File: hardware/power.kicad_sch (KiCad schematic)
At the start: 21 parts, among them J1 PWR_IN 12V, Q9 TPN1R603PL, U2 78L05

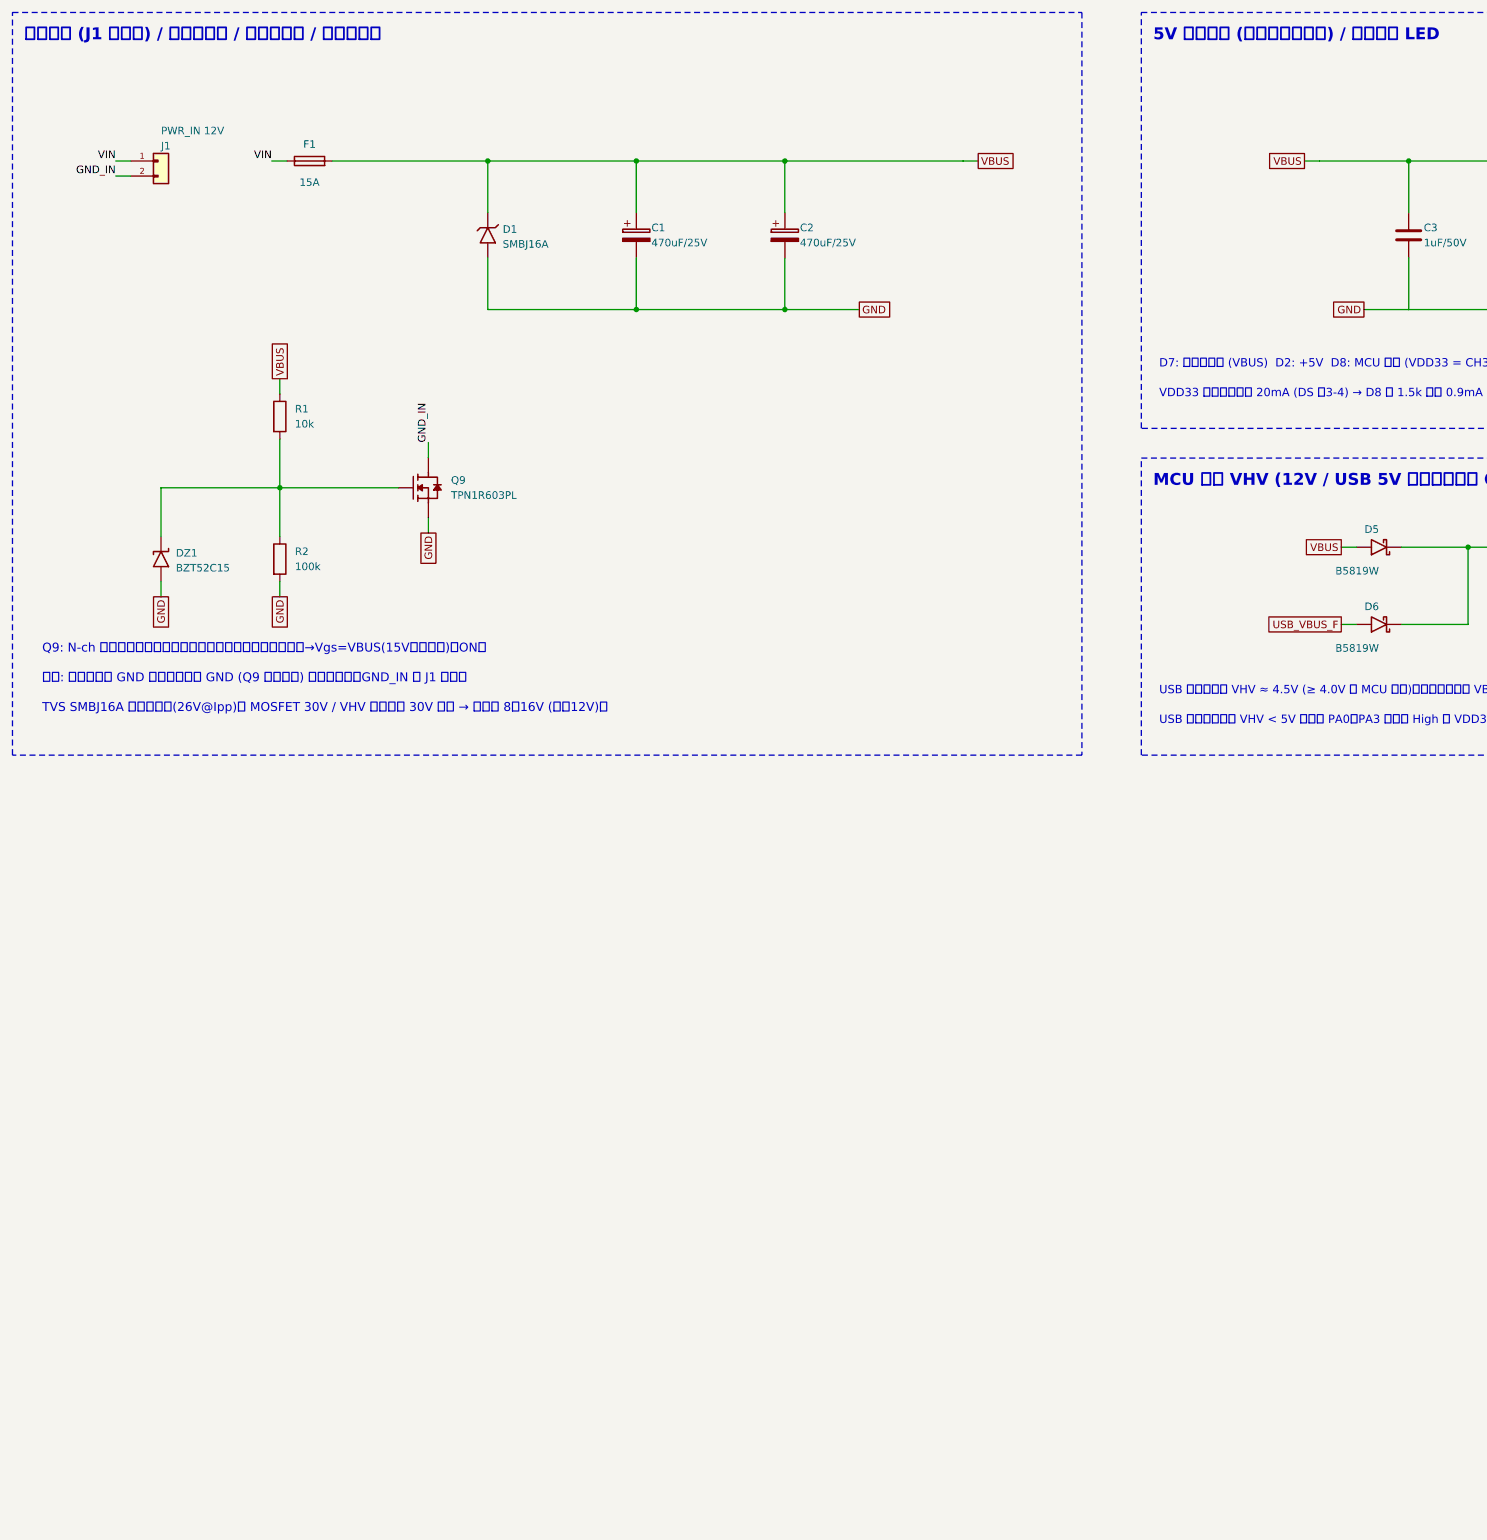
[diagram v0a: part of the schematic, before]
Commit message: Rev 0.2: 内蔵機能 (電流源/シンク・USB-PD・OPA/CMP 全モード) の活用
回路 (102/102 ネット一致):
- USB-PD シンクでモーター電源を供給: F3 → U5 LM74700 + Q10 → VBUS (PC3 で許可),
  USB VBUS 監視 (PA2), SMAJ20A。USBLC6 の基準を +3V3 に変更 (VBUS 20V 対策)
- J1 の逆接保護を U4 LM74700 + Q9 のハイサイド理想ダイオードに変更 (J1 / PD を安全に OR)
- 3 相センシングを PA5/PA6/PA7 に集約 (W 相 PA12 → PA6): CMP3 内部仮想中性点 + TIM2 捕捉
  によるセンサレス BEMF 検出, TIM2 ホール XOR, ISOURCE2 結線診断を同じピンで利用
- JP7: OPA3 入力を HB0 レッグ / バス電流で切替 (CMP2 + DAC でバス過電流・電流制限)
- JP8 + C105: QII1 (OPA1 → CMP1 → TIM3) でタコ / VR センサ / ブラシ DC 電流リップル計数
- 状態 LED を PC4 (USER/BOOT) と共用, J6/J7 を再割当 (1 線 SDI)

ファームウェア (警告 0):
- mpb.h ライブラリ: PD シンク (WCH USBPD_SNK 移植 + 8〜15V ポリシー + 給電パス制御),
  過電流保護 (CMP3/CMP2+DAC, TIM2 停止割込み), BEMF, ホール, タコ, NTC, 結線自己診断, TIM3 時間基準
- ブートローダ / テンプレートの状態 LED を PC4 (オープンドレイン) に変更

ドキュメント: docs/advanced_features.md (検討と判断, 要実機確認事項, Rev 0.3 候補)

Co-Authored-By: Claude Opus 5.5 <noreply@anthropic.com>
Claude-Session: https://claude.ai/code/session_01LENFjjhDfYjJZV1NWhB9uV
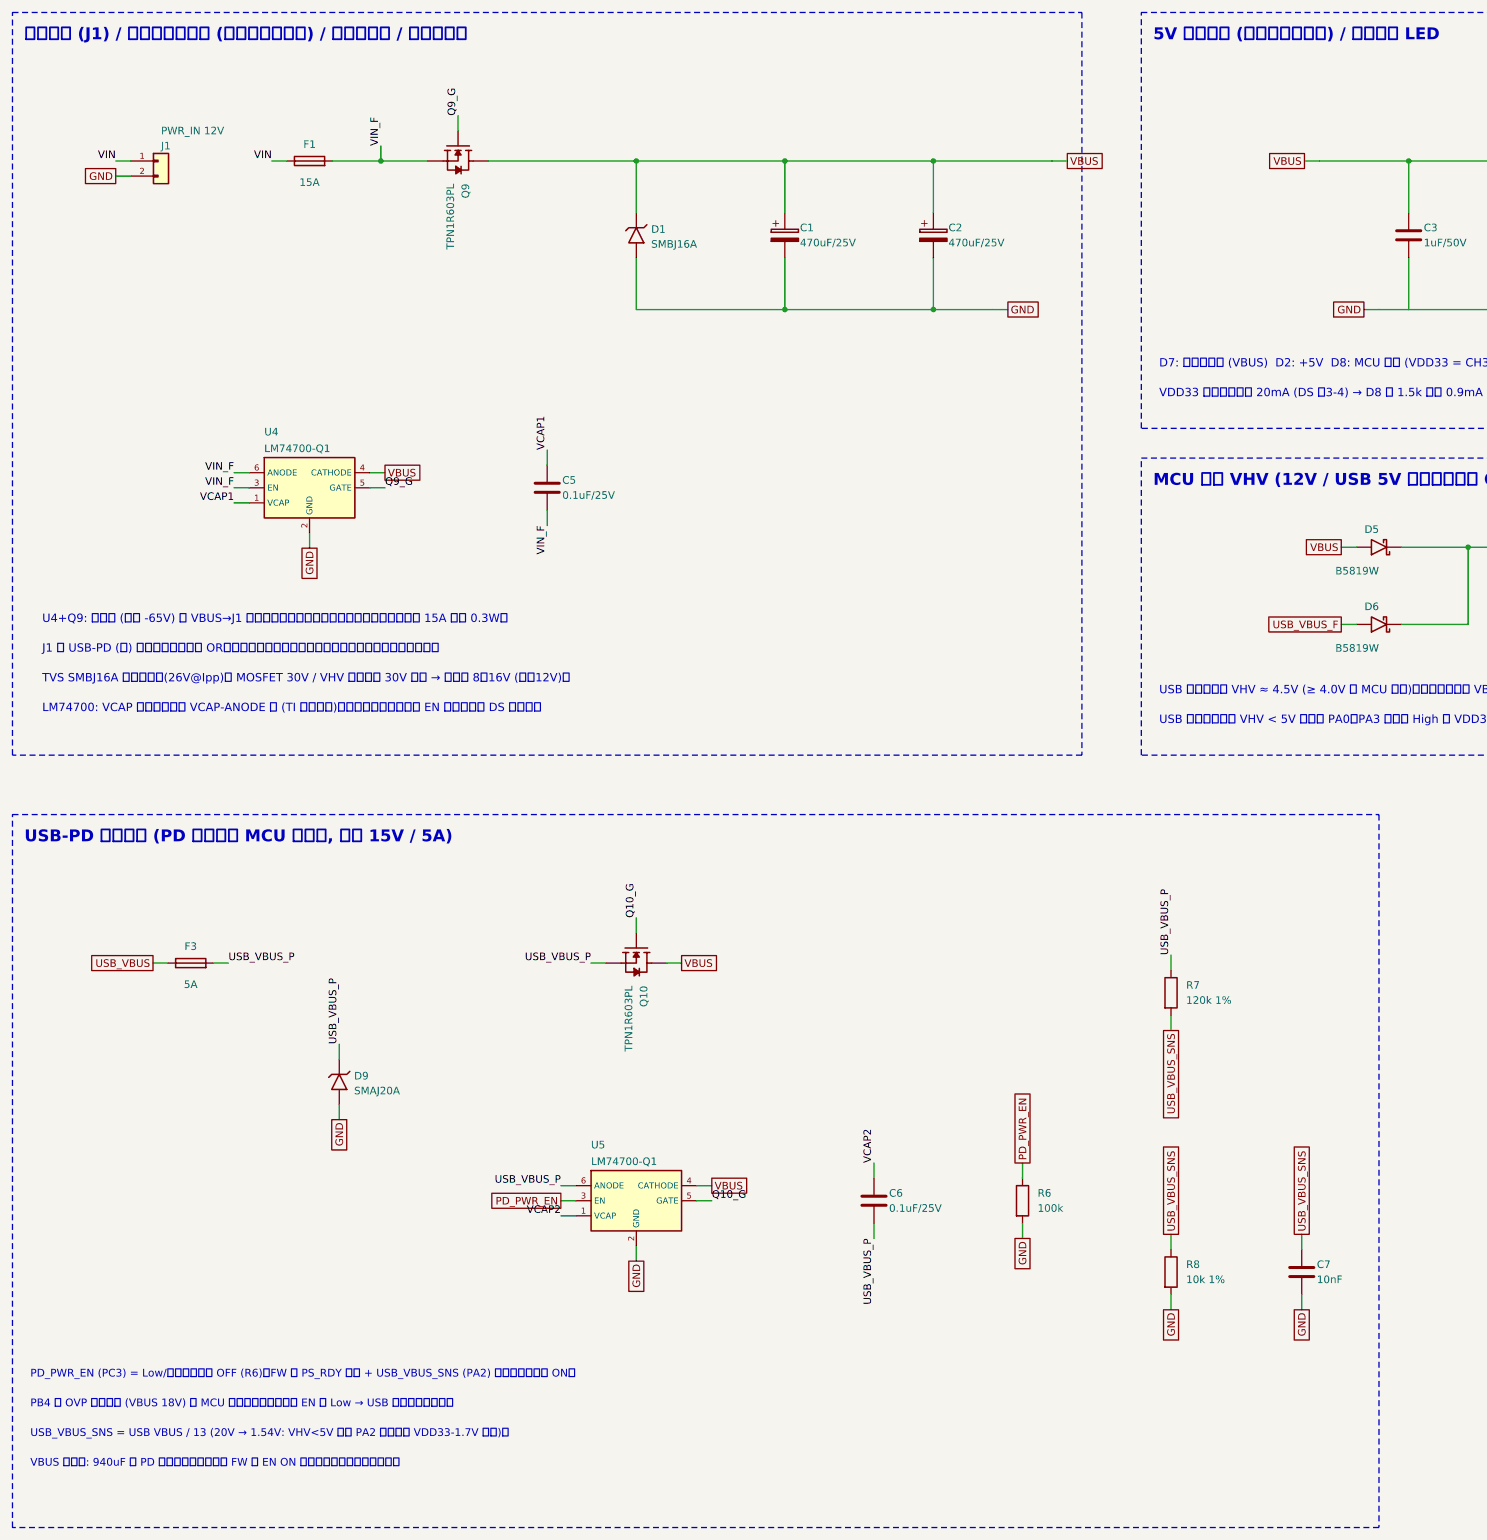
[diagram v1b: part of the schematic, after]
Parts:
- removed C1, C2: 470uF/25V, Capacitor_THT:CP_Radial_D10.0mm_P5.00mm, symbol mdrv:CP
- removed D1: SMBJ16A, Diode_SMD:D_SMB, symbol mdrv:D_TVS
- removed DZ1: BZT52C15, Diode_SMD:D_SOD-123, symbol mdrv:D_ZENER
- removed J1: PWR_IN 12V, TerminalBlock:TerminalBlock_bornier-2_P5.08mm, symbol mdrv:CONN2
- removed R1: 10k, Resistor_SMD:R_0402_1005Metric, symbol mdrv:R
- removed R2: 100k, Resistor_SMD:R_0402_1005Metric, symbol mdrv:R
- added C4: 1uF/25V, Capacitor_SMD:C_0603_1608Metric, symbol mdrv:C
- added C6: 0.1uF/25V, Capacitor_SMD:C_0603_1608Metric, symbol mdrv:C
- added C7: 10nF, Capacitor_SMD:C_0402_1005Metric, symbol mdrv:C
- added D2: GREEN 5V, LED_SMD:LED_0603_1608Metric, symbol mdrv:LED
- added D9: SMAJ20A, Diode_SMD:D_SMA, symbol mdrv:D_TVS
- added F1: 15A, Fuse:Fuseholder_Blade_Mini_Keystone_3568, symbol mdrv:FUSE
- added Q10: TPN1R603PL, Package_SO:Vishay_PowerPAK_1212-8_Single, symbol mdrv:NMOS
- added R3: 2.2k, Resistor_SMD:R_0402_1005Metric, symbol mdrv:R
- added R4: 10k, Resistor_SMD:R_0402_1005Metric, symbol mdrv:R
- added R6: 100k, Resistor_SMD:R_0402_1005Metric, symbol mdrv:R
- added R7: 120k 1%, Resistor_SMD:R_0402_1005Metric, symbol mdrv:R
- added R8: 10k 1%, Resistor_SMD:R_0402_1005Metric, symbol mdrv:R
- added U2: 78L05, Package_TO_SOT_SMD:SOT-89-3, symbol mdrv:REG3
- added U4, U5: LM74700-Q1, Package_TO_SOT_SMD:SOT-23-6, symbol mdrv:LM74700
- C1: renamed from R3; value 2.2k -> 470uF/25V; footprint Resistor_SMD:R_0402_1005Metric -> Capacitor_THT:CP_Radial_D10.0mm_P5.00mm; symbol mdrv:R -> mdrv:CP; MPN (none) -> 低ESR 電解/導電性高分子 470uF 25V
- C2: renamed from D2; value GREEN 5V -> 470uF/25V; footprint LED_SMD:LED_0603_1608Metric -> Capacitor_THT:CP_Radial_D10.0mm_P5.00mm; symbol mdrv:LED -> mdrv:CP; MPN (none) -> 低ESR 電解/導電性高分子 470uF 25V
- C5: renamed from U2; value 78L05 -> 0.1uF/25V; footprint Package_TO_SOT_SMD:SOT-89-3 -> Capacitor_SMD:C_0603_1608Metric; symbol mdrv:REG3 -> mdrv:C; MPN 78L05 (SOT-89, Vin max 30V) -> (none)
- D1: renamed from C4; value 1uF/25V -> SMBJ16A; footprint Capacitor_SMD:C_0603_1608Metric -> Diode_SMD:D_SMB; symbol mdrv:C -> mdrv:D_TVS; MPN (none) -> SMBJ16A (Vwm16V / Vc26V)
- F3: renamed from R4; value 10k -> 5A; footprint Resistor_SMD:R_0402_1005Metric -> Fuse:Fuse_1812_4532Metric; symbol mdrv:R -> mdrv:FUSE; MPN (none) -> 1812 5A 速断ヒューズ
- J1: renamed from F1; value 15A -> PWR_IN 12V; footprint Fuse:Fuseholder_Blade_Mini_Keystone_3568 -> TerminalBlock:TerminalBlock_bornier-2_P5.08mm; symbol mdrv:FUSE -> mdrv:CONN2; MPN ミニブレードヒューズ 15A -> 5.08mm 2P 端子台 (定格 ≥15A)
- Q9: MPN TPN1R603PL,L1Q (逆接続保護・ローサイド) -> TPN1R603PL,L1Q (J1 側 理想ダイオード)
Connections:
- net GND_IN is gone; now on net VBUS: Q9.5 (D)
- net +5V: now also C4.1, R3.1, U2.1 (OUT); no longer C1.1, C5.1 (OUT), D1.1
- net GND: now also C1.2, C2.2, J1.2 (P2), C4.2, C7.2, D2.1 (K), D9.2 (A), R6.2, R8.2, U2.2 (GND), U4.2 (GND), U5.2 (GND); no longer C2.1 (K), C5.2 (GND), Q9.1 (S), Q9.2 (S), Q9.3 (S)
- net VBUS: now also C1.1, C2.1, D1.1 (K), Q10.5 (D), R4.1, U2.3 (IN), U4.4 (CATHODE), U5.4 (CATHODE); no longer C5.3 (IN), F3.1, J1.2
- net VIN: now also F1.1
- net at D7.2 (A): now also R4.2; no longer F3.2
- net Q9_G: now reaches Q9.4 (G)
- net Q9_G: now also U4.5 (GATE)
- new net: D2.2 (A), R3.2
- new net PD_PWR_EN: R6.1, U5.3 (EN)
- new net Q10_G: Q10.4 (G), U5.5 (GATE)
- new net USB_VBUS: F3.1
- new net USB_VBUS_P: C6.2, D9.1 (K), F3.2, Q10.1 (S), Q10.2 (S), Q10.3 (S), R7.1, U5.6 (ANODE)
- new net USB_VBUS_SNS: C7.1, R7.2, R8.1
- new net VCAP1: C5.1, U4.1 (VCAP)
- new net VCAP2: C6.1, U5.1 (VCAP)
- new net VIN_F: C5.2, F1.2, Q9.1 (S), Q9.2 (S), Q9.3 (S), U4.3 (EN), U4.6 (ANODE)
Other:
- note added: "J1 と USB-PD (下) は理想ダイオード OR。両方あれば電圧の高い方が供給し、互いに逆流しない。"
- note added: "LM74700: VCAP コンデンサは VCAP-ANODE 間 (TI 推奨回路)。試作前にピン配置と EN しきい値を DS で確認。"
- note added: "PB4 の OVP リセット (VBUS 18V) で MCU がリセットされると EN も Low → USB 給電も自動遮断。"
- note added: "PD_PWR_EN (PC3) = Low/リセット中は OFF (R6)。FW は PS_RDY 受信 + USB_VBUS_SNS (PA2) で電圧確認後に ON。"
- note added: "U4+Q9: 逆接続 (最大 -65V) と VBUS→J1 への逆流を阻止する理想ダイオード。導通損失 15A で約 0.3W。"
- note added: "USB-PD 給電パス (PD 契約後に MCU が許可, 最大 15V / 5A)"
- note added: "USB_VBUS_SNS = USB VBUS / 13 (20V → 1.54V: VHV<5V 時の PA2 入力範囲 VDD33-1.7V 以内)。"
- note added: "VBUS の突入: 940uF を PD 電源で充電するため FW は EN ON 後に電流を段階的に上げる。"
- note added: "電源入力 (J1) / 理想ダイオード (逆接・逆流防止) / サージ保護 / バルク容量"
- note removed: "Q9: N-ch ローサイド逆接保護。正接続時はボディダイオード→Vgs=VBUS(15Vクランプ)でON。"
- note removed: "注意: 外部機器の GND は必ず基板側 GND (Q9 ソース側) を使うこと。GND_IN は J1 専用。"
- note removed: "電源入力 (J1 端子台) / 逆接続保護 / サージ保護 / バルク容量"
- moved on the sheet: C2, D1

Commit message: Rev 0.3: パワー段を子基板化 (A/B/C/D) し 2 層基板レイアウトを作成
構成:
- 主基板 (60x42mm, 2 層): 右 = CH32M030 / USB-C / GPIO・I2C・UART・SDI・HALL,
  左上 = 電源 (J1 → F1 → 理想ダイオード, USB-PD 経路), 左下 = 基板間コネクタ J9/J10 (裏面)
- 子基板と裏面同士を背中合わせに重ねる (基板間 約5mm, 裏面部品は高さ 2mm 以下)。
  RESET / USER・BOOT / センシング選択は主基板 TOP、電流チャネル選択 JP5/JP7 は子基板 TOP
- 子基板 A: TPN1R603PL (既存回路) / B: TKR74F04PB (24V 系, 66x66mm) /
  C: MTN2306AN3 (廉価版) / D: MOSFET なし (全信号をピンヘッダへ引き出し)
- 基板間ピンは同じ番号同士が嵌合 (ソケットを 270° 回転して裏面実装, 座標で全 32 ピンを検証)
- コネクタは USB-C 以外すべて 2.54mm ピンヘッダ。コンデンサは 1005/1608 基本
  (入手性を確認した量産品番。50V/10uF のみ 2012)
- 24V 対応: Q9 を 40V 品 (TPN2R304PL), VHV に 47Ω + 27V ツェナー, D1/R11 の 24V 用定数を注記,
  FW は make POWER_STAGE=B で VBUS 分圧比を切替
- F1 を NANO2 10A (SMD), スイッチを B3U-1000P に小型化

基板生成 (hardware/gen_pcb.py + pcblib.py):
- 配置 → Freerouting 1.9 自動配線 → 大電流ネットのベタ化 → GND ベタ・スティッチング
  → 残り接続の補修 (格子 A*, DRC が増えない経路のみ採用) → DRC
- 5 基板とも未接続 0・電気的 DRC エラー 0 (警告はシルクの重なりのみ)
- 製造データ hardware/fab/*.zip (ガーバー, ドリル, 両面の部品座標)

回路図: 主基板 82/82, 子基板 A/B/C 41/41, D 21/21 ネット一致。FW は A/B とも警告 0 でビルド。

Co-Authored-By: Claude Opus 5.5 <noreply@anthropic.com>
Claude-Session: https://claude.ai/code/session_01LENFjjhDfYjJZV1NWhB9uV
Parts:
- removed C1, C2: 470uF/25V, Capacitor_THT:CP_Radial_D10.0mm_P5.00mm, symbol mdrv:CP
- removed J1: PWR_IN 12V, TerminalBlock:TerminalBlock_bornier-2_P5.08mm, symbol mdrv:CONN2
- added C1: 10uF/50V, Capacitor_SMD:C_0805_2012Metric, symbol mdrv:C
- added D4: MMSZ5254B 27V, Diode_SMD:D_SOD-123, symbol mdrv:D_ZENER
- added J1: PWR_IN, Connector_PinHeader_2.54mm:PinHeader_2x04_P2.54mm_Vertical, symbol mdrv:CONN2x4
- C3: footprint Capacitor_SMD:C_0805_2012Metric -> Capacitor_SMD:C_0603_1608Metric; MPN (none) -> Murata GRM188R61H105KAALD (X5R 1608)
- C4: footprint Capacitor_SMD:C_0603_1608Metric -> Capacitor_SMD:C_0402_1005Metric; MPN (none) -> Murata GRM155R61E105KA12D (X5R 1005)
- C5, C6: value 0.1uF/25V -> 0.1uF/50V; footprint Capacitor_SMD:C_0603_1608Metric -> Capacitor_SMD:C_0402_1005Metric; MPN (none) -> Murata GRM155R71H104KE14D (X7R 1005)
- C7: value 10nF -> 10nF/50V; MPN (none) -> Murata GRM155R71H103KA88D (X7R 1005)
- D1: MPN SMBJ16A (Vwm16V / Vc26V) -> SMBJ16A (12V 系) / 24V 系は SMBJ24A に変更
- D9: MPN SMAJ20A (USB 側 ESD/サージ, PD 20V まで許容) -> SMAJ20A (USB 側サージ)
- F1: value 15A -> 10A; footprint Fuse:Fuseholder_Blade_Mini_Keystone_3568 -> mPB:Fuse_Littelfuse_NANO2_2410; MPN ミニブレードヒューズ 15A -> Littelfuse 0451010.MRL (NANO2 2410, 10A 速断)
- F3: MPN 1812 5A 速断ヒューズ -> 1812 5A 速断ヒューズ (例: Bourns SF-1812F500)
- Q10: MPN TPN1R603PL,L1Q (USB 側 理想ダイオード) -> Toshiba TPN1R603PL,L1Q (USB 側 理想ダイオード)
- Q9: value TPN1R603PL -> TPN2R304PL; MPN TPN1R603PL,L1Q (J1 側 理想ダイオード) -> Toshiba TPN2R304PL,L1Q (40V 2.3mΩ, J1 側 理想ダイオード)
- R10: value 10R -> 47R; footprint Resistor_SMD:R_0402_1005Metric -> Resistor_SMD:R_0603_1608Metric
- R4: value 10k -> 15k
- U2: MPN 78L05 (SOT-89, Vin max 30V) -> 78L05 (SOT-89, Vin ≤30V)
- U4, U5: MPN TI LM74700-Q1 (DBV) -> TI LM74700QDBVRQ1
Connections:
- net GND: now also C1.2, D4.2 (A), J1.2 (P2), J1.4 (P4), J1.6 (P6), J1.8 (P8)
- net VBUS: now also C1.1
- net VHV: now also D4.1 (K)
- net VIN: now also J1.1 (P1), J1.3 (P3), J1.5 (P5), J1.7 (P7)
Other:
- note added: "12V 系: D1=SMBJ16A, R11=110k (OVP 18V)。24V 系 (子基板 B): D1=SMBJ24A, R11=180k (OVP 28.5V)。"
- note added: "CH32M030 の VS 絶対最大 30V / VHV 動作 5〜28V → 24V 系は安定化電源専用 (回生・サージで 28V を超えないこと)。"
- note added: "D7: モータ電源 (VBUS, 12V で 0.6mA / 24V で 1.5mA) D2: +5V D8: MCU 電源 (VDD33)"
- note added: "J1 と USB-PD (下) は理想ダイオード OR。バルク容量は子基板の MOSFET 近傍に置く (C1 は局所バイパス)。"
- note added: "J1 はピンヘッダ 4 ピン並列 (約 10A)。それ以上は J1 のランドへ線材を直接はんだ付けする。"
- note added: "MCU 電源 VHV (VBUS / USB 5V のダイオード OR + 27V クランプ)"
- note added: "PB4 の OVP リセットで MCU がリセットされると EN も Low → USB 給電も自動遮断。"
- note added: "R10 47Ω + D4 27V: 24V 系のサージで VHV が 30V を超えないようにする (MCU 消費 ≤35mA で降下 ≤1.7V)。"
- note added: "U4+Q9: 逆接続 (最大 -65V) と VBUS→J1 への逆流を阻止する理想ダイオード。Q9 は 40V 品 (24V 系と共通)。"
- note added: "USB のみ給電では VHV < 5V となり PA0〜PA3 の出力 High が VDD33-1.7V に下がる (DS 注5)。"
- note added: "USB のみ給電時 VHV ≈ 4.4V (≥ 4.0V で MCU 動作)。ゲート駆動は VBUS ≥ 8V を FW で確認してから許可。"
- note added: "USB_VBUS_SNS = USB VBUS / 13 (20V → 1.54V)。"
- note added: "VBUS の突入: 子基板のバルク容量を PD 電源で充電するため FW は EN ON 後に電流を段階的に上げる。"
- note added: "電源入力 (J1 2x4 ピン) / 理想ダイオード (逆接・逆流防止) / サージ保護"
- note removed: "D7: モータ電源 (VBUS) D2: +5V D8: MCU 電源 (VDD33 = CH32M030 内蔵 LDO 出力)"
- note removed: "J1 と USB-PD (下) は理想ダイオード OR。両方あれば電圧の高い方が供給し、互いに逆流しない。"
- note removed: "LM74700: VCAP コンデンサは VCAP-ANODE 間 (TI 推奨回路)。試作前にピン配置と EN しきい値を DS で確認。"
- note removed: "MCU 電源 VHV (12V / USB 5V のダイオード OR)"
- note removed: "PB4 の OVP リセット (VBUS 18V) で MCU がリセットされると EN も Low → USB 給電も自動遮断。"
- note removed: "TVS SMBJ16A のクランプ(26V@Ipp)は MOSFET 30V / VHV 絶対最大 30V 未満 → 入力は 8〜16V (公称12V)。"
- note removed: "U4+Q9: 逆接続 (最大 -65V) と VBUS→J1 への逆流を阻止する理想ダイオード。導通損失 15A で約 0.3W。"
- note removed: "USB のみ給電では VHV < 5V となり PA0〜PA3 の出力 High が VDD33-1.7V に下がる (DS 注5)。書込みは 12V 給電を推奨。"
- note removed: "USB のみ給電時 VHV ≈ 4.5V (≥ 4.0V で MCU 動作)。ゲート駆動は VBUS ≥ 8V を FW で確認してから許可。"
- note removed: "USB_VBUS_SNS = USB VBUS / 13 (20V → 1.54V: VHV<5V 時の PA2 入力範囲 VDD33-1.7V 以内)。"
- note removed: "VBUS の突入: 940uF を PD 電源で充電するため FW は EN ON 後に電流を段階的に上げる。"
- note removed: "電源入力 (J1) / 理想ダイオード (逆接・逆流防止) / サージ保護 / バルク容量"
- title: mPBCH32M030DS0  CH32M030 Universal Motor Driver -> mPBCH32M030DS0  CH32M030 Universal Motor Driver - Main board
